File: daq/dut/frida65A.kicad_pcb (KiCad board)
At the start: 4 copper layers, 100 x 100 mm, 64 parts, among them J1 TP_PWR, J10 TP_LOGIC, J11 TP_OUT, J2 CONN_IN_P, J3 CONN_IN_N, J4 TP_CFG, J5 CONN_CFG, J6 TP_IN, J7 TP_INIT, J8 TP_SAMP, J9 TP_COMP, U1 DUT, U2 THS4520RGTT

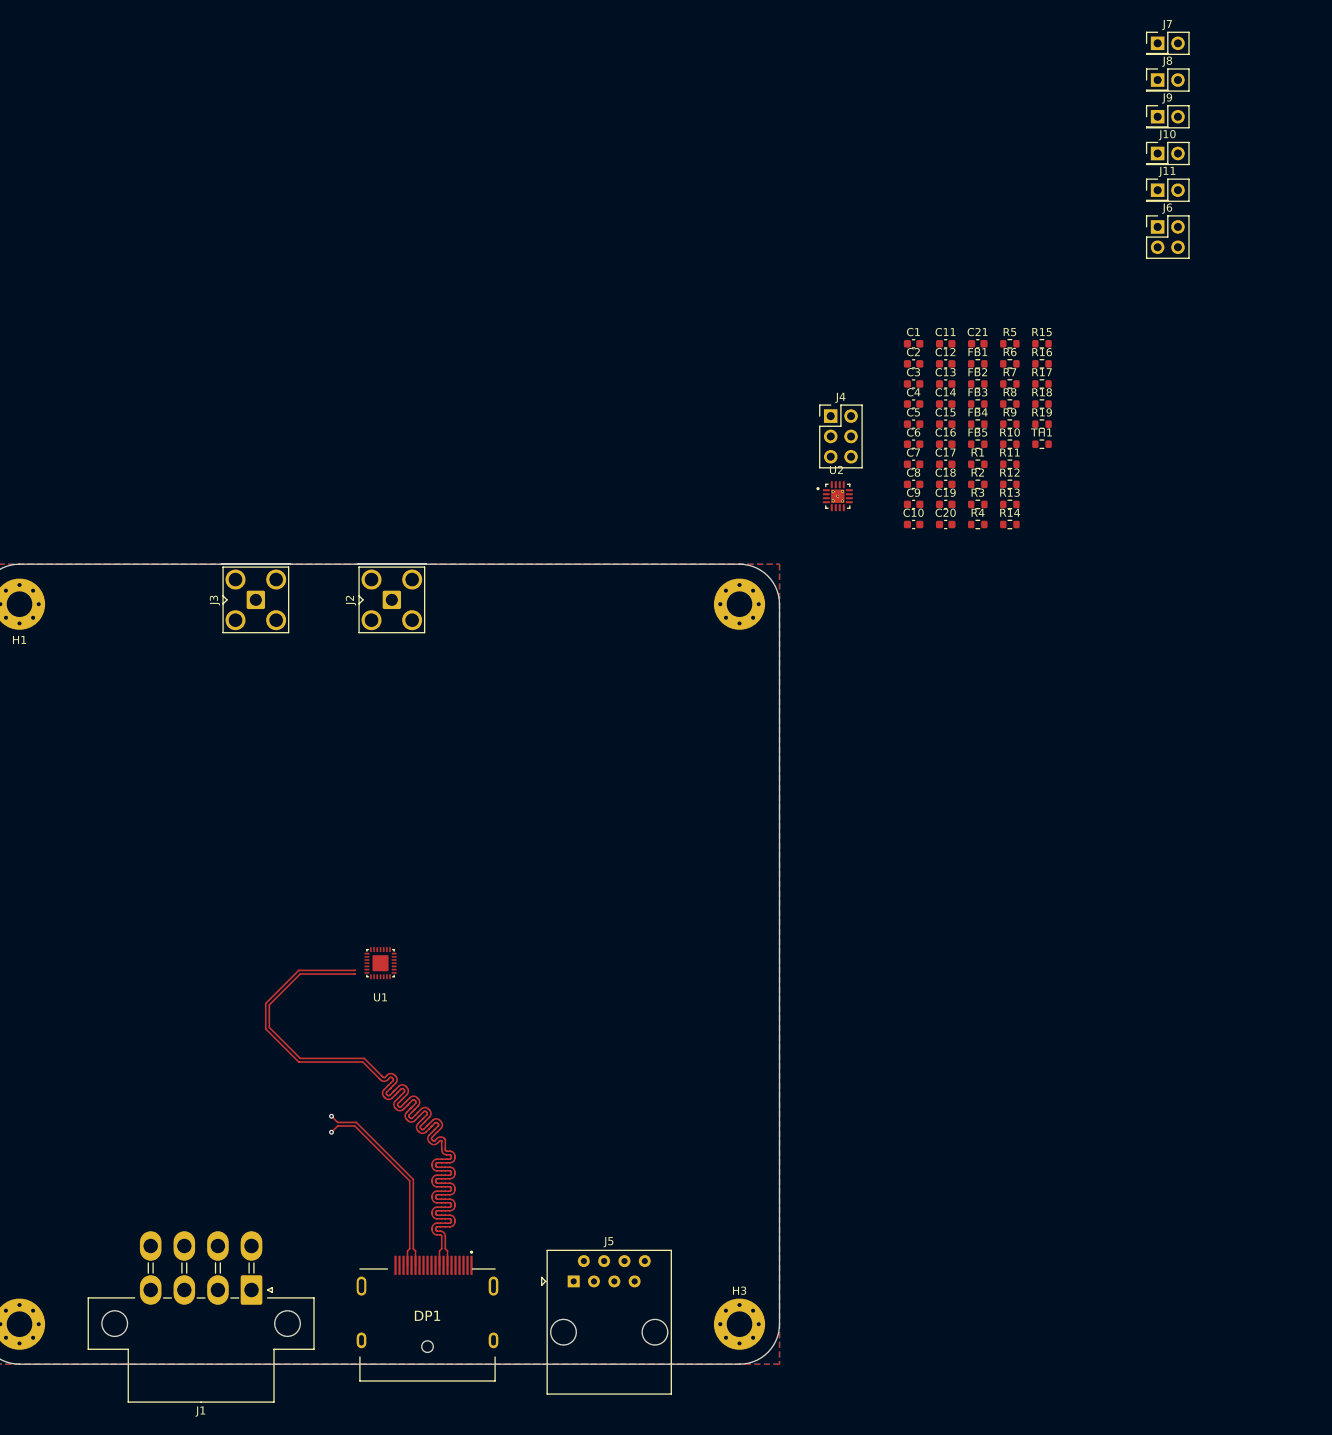
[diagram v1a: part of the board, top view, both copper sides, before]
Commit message: Update PCB schematic, and differential layout traces
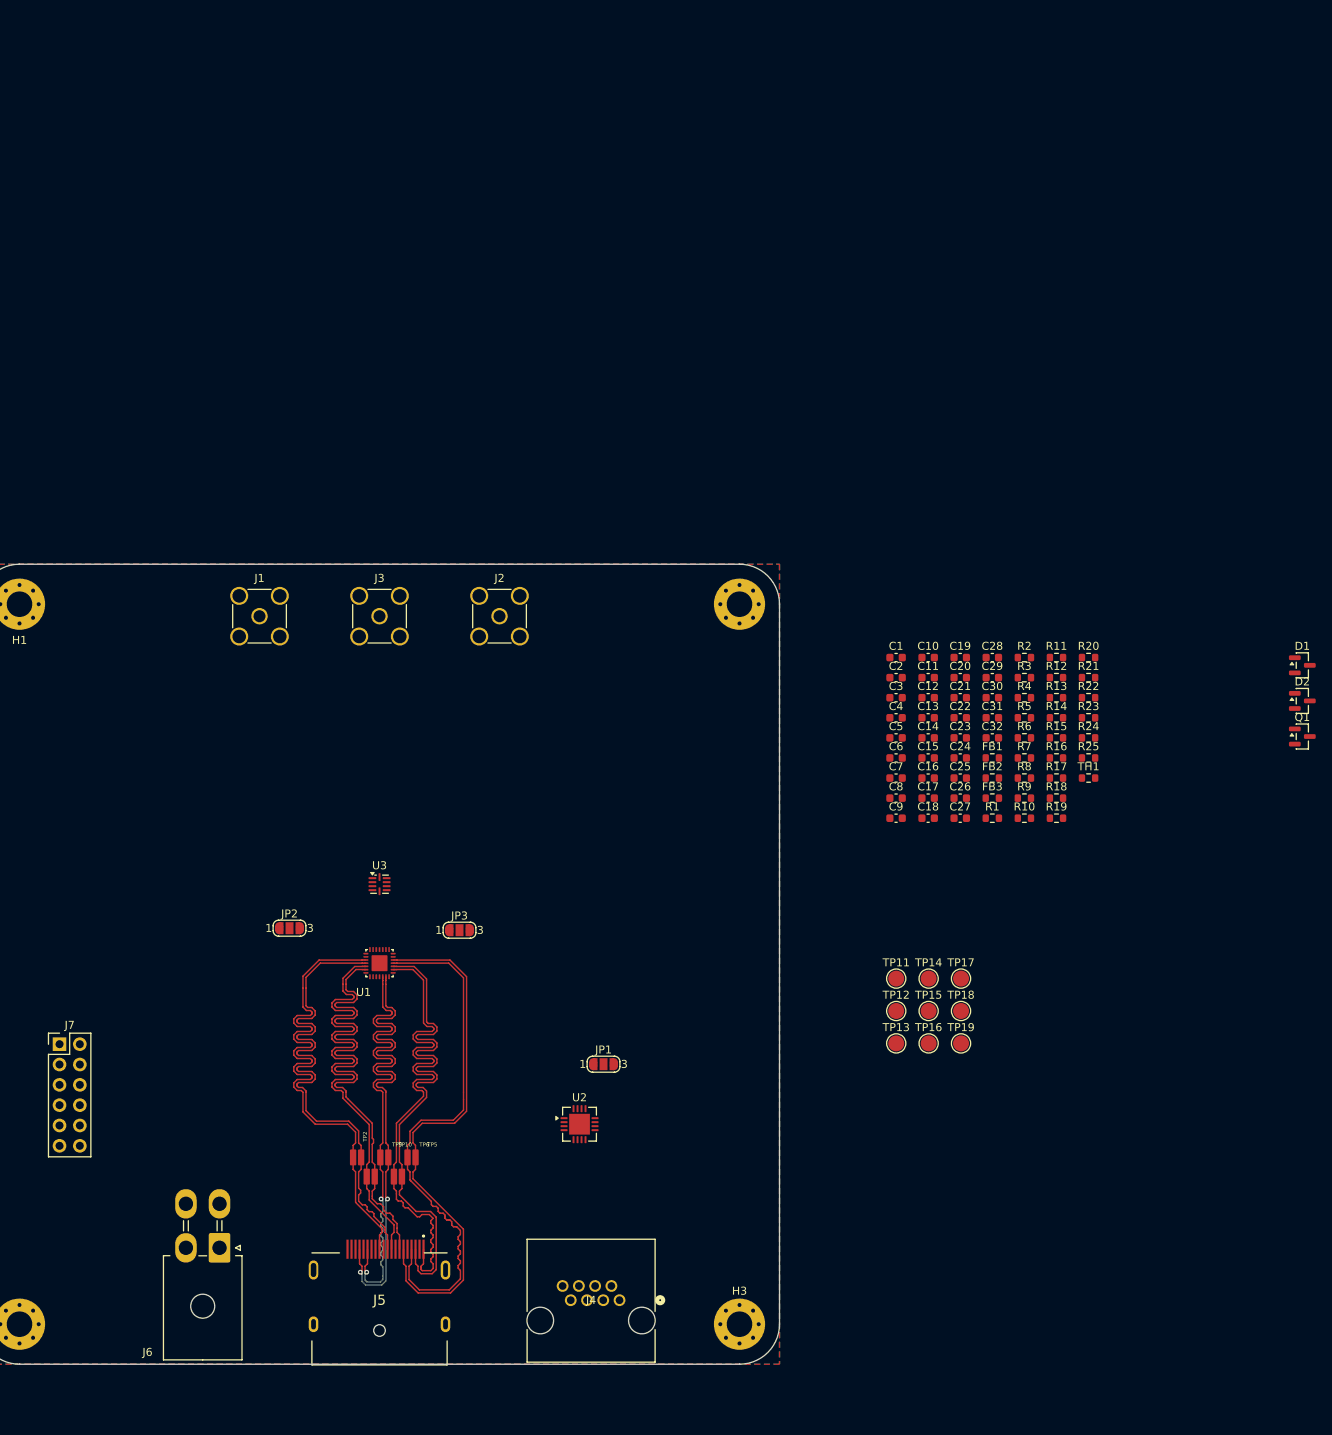
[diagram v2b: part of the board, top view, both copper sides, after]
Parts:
- removed DP1: DP, frida:Molex_DisplayPort_472720024
- removed FB4, FB5: FerriteBead_Small, Resistor_SMD:R_0603_1608Metric
- removed J10: TP_LOGIC, Connector_PinHeader_2.54mm:PinHeader_2x01_P2.54mm_Vertical
- removed J11: TP_OUT, Connector_PinHeader_2.54mm:PinHeader_2x01_P2.54mm_Vertical
- removed J8: TP_SAMP, Connector_PinHeader_2.54mm:PinHeader_2x01_P2.54mm_Vertical
- removed J9: TP_COMP, Connector_PinHeader_2.54mm:PinHeader_2x01_P2.54mm_Vertical
- added C22: 47u, Capacitor_SMD:C_0603_1608Metric, F.Cu at (222.6, 69.2)
- added C23: 1u, Capacitor_SMD:C_0603_1608Metric, F.Cu at (222.6, 71.7)
- added C24: 100n, Capacitor_SMD:C_0603_1608Metric, F.Cu at (222.6, 74.2)
- added C25: 100n, Capacitor_SMD:C_0603_1608Metric, F.Cu at (222.6, 76.7)
- added C26: 1u, Capacitor_SMD:C_0603_1608Metric, F.Cu at (222.6, 79.2)
- added C27: 100n, Capacitor_SMD:C_0603_1608Metric, F.Cu at (222.6, 81.8)
- added C28: 1u, Capacitor_SMD:C_0603_1608Metric, F.Cu at (226.6, 61.7)
- added C29: 100n, Capacitor_SMD:C_0603_1608Metric, F.Cu at (226.6, 64.2)
- added C30: 51pF, Capacitor_SMD:C_0603_1608Metric, F.Cu at (226.6, 66.7)
- added C31: 100n, Capacitor_SMD:C_0603_1608Metric, F.Cu at (226.6, 69.2)
- added C32: 1u, Capacitor_SMD:C_0603_1608Metric, F.Cu at (226.6, 71.7)
- added D1: BAV99, Package_TO_SOT_SMD:SOT-23, F.Cu at (265.4, 62.6)
- added D2: BAV99, Package_TO_SOT_SMD:SOT-23, F.Cu at (265.4, 67.1)
- added JP1: SolderJumper_3_Open, Jumper:SolderJumper-3_P1.3mm_Open_RoundedPad1.0x1.5mm_NumberLabels, F.Cu at (178.0, 112.5)
- added JP2: SolderJumper_3_Open, Jumper:SolderJumper-3_P1.3mm_Open_RoundedPad1.0x1.5mm_NumberLabels, F.Cu at (138.8, 95.5)
- added JP3: SolderJumper_3_Open, Jumper:SolderJumper-3_P1.3mm_Open_RoundedPad1.0x1.5mm_NumberLabels, F.Cu at (160.0, 95.8)
- added Q1: NMOS, Package_TO_SOT_SMD:SOT-23, F.Cu at (265.4, 71.5)
- added R20: 1k, Resistor_SMD:R_0603_1608Metric, F.Cu at (238.6, 61.7)
- added R21: 1k, Resistor_SMD:R_0603_1608Metric, F.Cu at (238.6, 64.2)
- added R22: 499, Resistor_SMD:R_0603_1608Metric, F.Cu at (238.6, 66.7)
- added R23: 499, Resistor_SMD:R_0603_1608Metric, F.Cu at (238.6, 69.2)
- added R24: 499, Resistor_SMD:R_0603_1608Metric, F.Cu at (238.6, 71.7)
- added R25: 499, Resistor_SMD:R_0603_1608Metric, F.Cu at (238.6, 74.2)
- added TP1: TestPoint Keystone 5001, frida:Test_Point, F.Cu at (146.7, 124.2)
- added TP10: TestPoint Keystone 5001, frida:Test_Point, F.Cu at (151.1, 124.2)
- added TP11: TestPoint, TestPoint:TestPoint_Pad_D2.0mm, F.Cu at (214.6, 101.8)
- added TP12: TestPoint, TestPoint:TestPoint_Pad_D2.0mm, F.Cu at (214.6, 105.8)
- added TP13: TestPoint, TestPoint:TestPoint_Pad_D2.0mm, F.Cu at (214.6, 109.9)
- added TP14: TestPoint, TestPoint:TestPoint_Pad_D2.0mm, F.Cu at (218.6, 101.8)
- added TP15: TestPoint, TestPoint:TestPoint_Pad_D2.0mm, F.Cu at (218.6, 105.8)
- added TP16: TestPoint, TestPoint:TestPoint_Pad_D2.0mm, F.Cu at (218.6, 109.9)
- added TP17: TestPoint, TestPoint:TestPoint_Pad_D2.0mm, F.Cu at (222.7, 101.8)
- added TP18: TestPoint, TestPoint:TestPoint_Pad_D2.0mm, F.Cu at (222.7, 105.8)
- added TP19: TestPoint, TestPoint:TestPoint_Pad_D2.0mm, F.Cu at (222.7, 109.9)
- added TP2: TestPoint Keystone 5001, frida:Test_Point, F.Cu at (147.7, 124.2)
- added TP3: TestPoint Keystone 5001, frida:Test_Point, F.Cu at (148.4, 126.5)
- added TP4: TestPoint Keystone 5001, frida:Test_Point, F.Cu at (149.4, 126.5)
- added TP5: TestPoint Keystone 5001, frida:Test_Point, F.Cu at (154.5, 124.2)
- added TP6: TestPoint Keystone 5001, frida:Test_Point, F.Cu at (153.5, 124.2)
- added TP7: TestPoint Keystone 5001, frida:Test_Point, F.Cu at (152.8, 126.5)
- added TP8: TestPoint Keystone 5001, frida:Test_Point, F.Cu at (151.8, 126.5)
- added TP9: TestPoint Keystone 5001, frida:Test_Point, F.Cu at (150.1, 124.2)
- added U3: DiffAmp TI THS4541, frida:TI_DiffAmp_THS4541, F.Cu at (150.0, 90.0)
- J1: value TP_PWR -> SMA Molex 733910070; footprint frida:Molex_MiniFitJr_469990014 -> frida:Molex_SMA_733910070
- J2: value CONN_IN_P -> SMA Molex 733910070; footprint Connector_Coaxial:SMA_Amphenol_901-143_Horizontal -> frida:Molex_SMA_733910070
- J3: value CONN_IN_N -> SMA Molex 733910070; footprint Connector_Coaxial:SMA_Amphenol_901-143_Horizontal -> frida:Molex_SMA_733910070
- J4: value TP_CFG -> RJ45 Molex 446200002; footprint Connector_PinHeader_2.54mm:PinHeader_2x03_P2.54mm_Vertical -> frida:Molex_RJ45_446200002
- J5: value CONN_CFG -> DisplayPort Molex 472720024; footprint Connector_RJ:RJ45_Amphenol_54602-x08_Horizontal -> frida:Molex_DisplayPort_472720024
- J6: value TP_IN -> MiniFitJr Molex 469990014; footprint Connector_PinHeader_2.54mm:PinHeader_2x02_P2.54mm_Vertical -> frida:Molex_MiniFitJr_469990014
- J7: value TP_INIT -> Conn_02x06_Top_Bottom; footprint Connector_PinHeader_2.54mm:PinHeader_2x01_P2.54mm_Vertical -> Connector_PinHeader_2.54mm:PinHeader_2x06_P2.54mm_Vertical
- R14, R15: value 499 -> 54.9
- R16: value 499 -> 10k
- R17: value 499 -> 50
- R18, R19: value 1k -> 499
- U1: value DUT -> ASIC FRIDA 65A
- U2: value THS4520RGTT -> LevelShifter TI TXV0106Q1; footprint frida:QFN50P300X300X100-17N -> frida:TI_LevelShifter_TXV0106Q1
- moved J7 185.7 mm to (110.0, 110.0)
- moved J6 173.3 mm to (130.0, 135.4), turned to 180 degrees
- moved J4 113.6 mm to (180.0, 142.0)
- moved U2 84.9 mm to (175.0, 120.0)
- moved J1 84.2 mm to (135.0, 56.5), turned to 0 degrees
- moved FB2 49.3 mm to (226.6, 76.7)
- moved R17 49.3 mm to (234.6, 76.7)
- moved FB1 49.3 mm to (226.6, 74.2)
- moved R16 49.3 mm to (234.6, 74.2)
- moved R19 49.3 mm to (234.6, 81.8)
- moved FB3 49.3 mm to (226.6, 79.2)
- moved R15 49.3 mm to (234.6, 71.7)
- moved R18 49.3 mm to (234.6, 79.2)
- moved R10 46.8 mm to (230.6, 81.8)
- moved R5 46.8 mm to (230.6, 69.2)
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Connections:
- C18 pad 1: /VDD_DIF -> /VS_N
- C19 pad 1: /VDD_DIF -> /VS_N
- C20 pad 1: /VDD_DIF -> /VS_N
- C21 pad 1: /VDD_DIF -> /VS_N
- FB1 pad 1: Net-(J17-Pin_1) -> Net-(FB1-Pad1)
- FB1 pad 2: /VDD_D -> /VDD
- FB2 pad 1: Net-(J17-Pin_2) -> Net-(FB2-Pad1)
- FB2 pad 2: /VDD_A -> Net-(J7-Pin_5)
- FB3 pad 1: Net-(J17-Pin_3) -> Net-(FB3-Pad1)
- FB3 pad 2: /VDD_DAC -> Net-(J7-Pin_6)
- J1 pad 1: /VDD_D -> GND
- J1 pad 2: /VDD_A -> /VIN_P_EXT
- J2 pad 1: /VIN_P_EXT -> GND
- J2 pad 2: GND -> /VIN_N_EXT
- J3 pad 1: /VIN_N_EXT -> GND
- J3 pad 2: GND -> /VOCM_EXT
- J4 pad 1: /SPI_CS_B -> /SPI_CS_B_EXT
- J4 pad 2: /SPI_SDO -> /SPI_SDO_EXT
- J4 pad 3: /SPI_SDI -> /SPI_SDI_EXT
- J4 pad 4: /SPI_SCLK -> /SPI_SCLK_EXT
- J4 pad 5: /RST_B -> /RST_B_EXT
- J4 pad 6: GND -> /AMP_EN_EXT_B
- J5 pad 1: /SPI_CS_B -> /CLK_LOGIC_N
- J5 pad 2: /SPI_SDO -> GND
- J5 pad 3: /SPI_SDI -> /CLK_LOGIC_P
- J5 pad 4: /SPI_SCLK -> /CLK_COMP_N
- J5 pad 5: /RST_B -> GND
- J5 pad 6: /AMP_EN -> /CLK_COMP_P
- J5 pad 7: unconnected-(J5-Pad7) -> /CLK_SAMP_N
- J5 pad 8: unconnected-(J5-Pad8) -> GND
- J6 pad 1: Net-(J16-Pin_3) -> Net-(FB1-Pad1)
- J6 pad 2: Net-(J16-Pin_3) -> Net-(FB2-Pad1)
- J6 pad 3: GND -> Net-(FB3-Pad1)
- J7 pad 1: /CLK_INIT_P -> /VDD
- J7 pad 2: /CLK_INIT_N -> /VDD
- R10 pad 1: /CLK_COMP_N -> /CLK_SAMP_P
- R11 pad 1: /CLK_LOGIC_P -> /CLK_INIT_N
- R12 pad 1: /CLK_LOGIC_N -> /CLK_INIT_P
- R14 pad 1: Net-(U2-VIN-) -> GND
- R14 pad 2: Net-(J12-Pin_1) -> /VIN_P_EXT
- R15 pad 1: Net-(U2-VIN+) -> GND
- R15 pad 2: Net-(J16-Pin_1) -> Net-(JP1-C)
- R16 pad 1: unconnected-(R16-Pad1) -> /VS_P
- R16 pad 2: Net-(U2-VIN+) -> /AMP_EN
- R17 pad 1: unconnected-(R17-Pad1) -> GND
- R17 pad 2: Net-(U2-VIN-) -> Net-(JP1-A)
- R18 pad 1: GND -> Net-(U3-IN-)
- R18 pad 2: /AMP_EN -> Net-(JP1-C)
- R19 pad 1: Net-(U2-~{PD}) -> Net-(U3-IN+)
- R19 pad 2: GND -> /VIN_P_EXT
- R5 pad 1: /CLK_INIT_P -> /CLK_LOGIC_N
- R6 pad 1: /CLK_INIT_N -> /CLK_LOGIC_P
- R7 pad 1: /CLK_SAMP_P -> /CLK_COMP_N
- R8 pad 1: /CLK_SAMP_N -> /CLK_COMP_P
- R9 pad 1: /CLK_COMP_P -> /CLK_SAMP_N
- TH1 pad 1: Net-(DP1-Pad13) -> Net-(J5-Pad13)
- TH1 pad 2: Net-(DP1-Pad14) -> Net-(J5-Pad14)
- U1 pad 24: Net-(J16-Pin_3) -> /VIN_N
- U1 pad 25: Net-(J12-Pin_3) -> /VIN_P
- U2 pad 1: (no net) -> /VDD_DAQ
- U2 pad 10: Net-(J16-Pin_1) -> unconnected-(U2-B6-Pad10)
- U2 pad 11: Net-(U2-VIN+) -> /SPI_CS_B
- U2 pad 12: Net-(U2-~{PD}) -> /SPI_SDO
- U2 pad 13: GND -> /SPI_SDI
- U2 pad 14: GND -> /SPI_SCLK
- U2 pad 15: GND -> /RST_B
- U2 pad 16: GND -> /VDD_IO
- U2 pad 2: Net-(U2-VIN-) -> /RST_B_EXT
- U2 pad 3: Net-(J12-Pin_1) -> /SPI_SCLK_EXT
- U2 pad 4: unconnected-(U2-CM-Pad4) -> /SPI_SDI_EXT
- U2 pad 5: /VDD_DIF -> /SPI_SDO_EXT
- U2 pad 6: /VDD_DIF -> /SPI_CS_B_EXT
- U2 pad 7: /VDD_DIF -> unconnected-(U2-A6-Pad7)
- U2 pad 8: /VDD_DIF -> GND
- U2 pad 9: unconnected-(U2-CM__1-Pad9) -> GND
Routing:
- net /CLK_COMP_P: track 0.00 -> 68.5 mm
- net /CLK_INIT_N: track 0.00 -> 68.5 mm
- net /CLK_COMP_N: track 0.00 -> 68.5 mm
- net /CLK_INIT_P: track 0.00 -> 68.5 mm
- net /CLK_LOGIC_N: track 0.00 -> 68.5 mm
- net /CLK_LOGIC_P: track 0.00 -> 68.5 mm
- net /CLK_SAMP_P: track 99.3 -> 68.5 mm
- net /CLK_SAMP_N: track 98.5 -> 68.5 mm
- net /COMP_OUT_N: track 44.9 -> 65.4 mm, vias 1 -> 2
- net /COMP_OUT_P: track 45.3 -> 65.4 mm, vias 1 -> 2

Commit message: Remove solder mask from footprints
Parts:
- J7: value Conn_02x06_Top_Bottom -> Conn_02x06_Odd_Even
- moved J7 25.6 mm to (85.5, 117.3)
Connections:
- FB2 pad 2: Net-(J7-Pin_5) -> Net-(J7-Pin_9)
- FB3 pad 2: Net-(J7-Pin_6) -> Net-(J7-Pin_11)
- J7 pad 10: /VDD_DAC -> /VS_P
- J7 pad 11: /VS_P -> Net-(J7-Pin_11)
- J7 pad 2: /VDD -> /VDD_A
- J7 pad 4: /VDD -> /VDD_IO
- J7 pad 5: Net-(J7-Pin_5) -> /VDD
- J7 pad 6: Net-(J7-Pin_6) -> /VDD_D
- J7 pad 7: /VDD_A -> /VDD
- J7 pad 8: /VDD_IO -> /VDD_DAC
- J7 pad 9: /VDD_D -> Net-(J7-Pin_9)

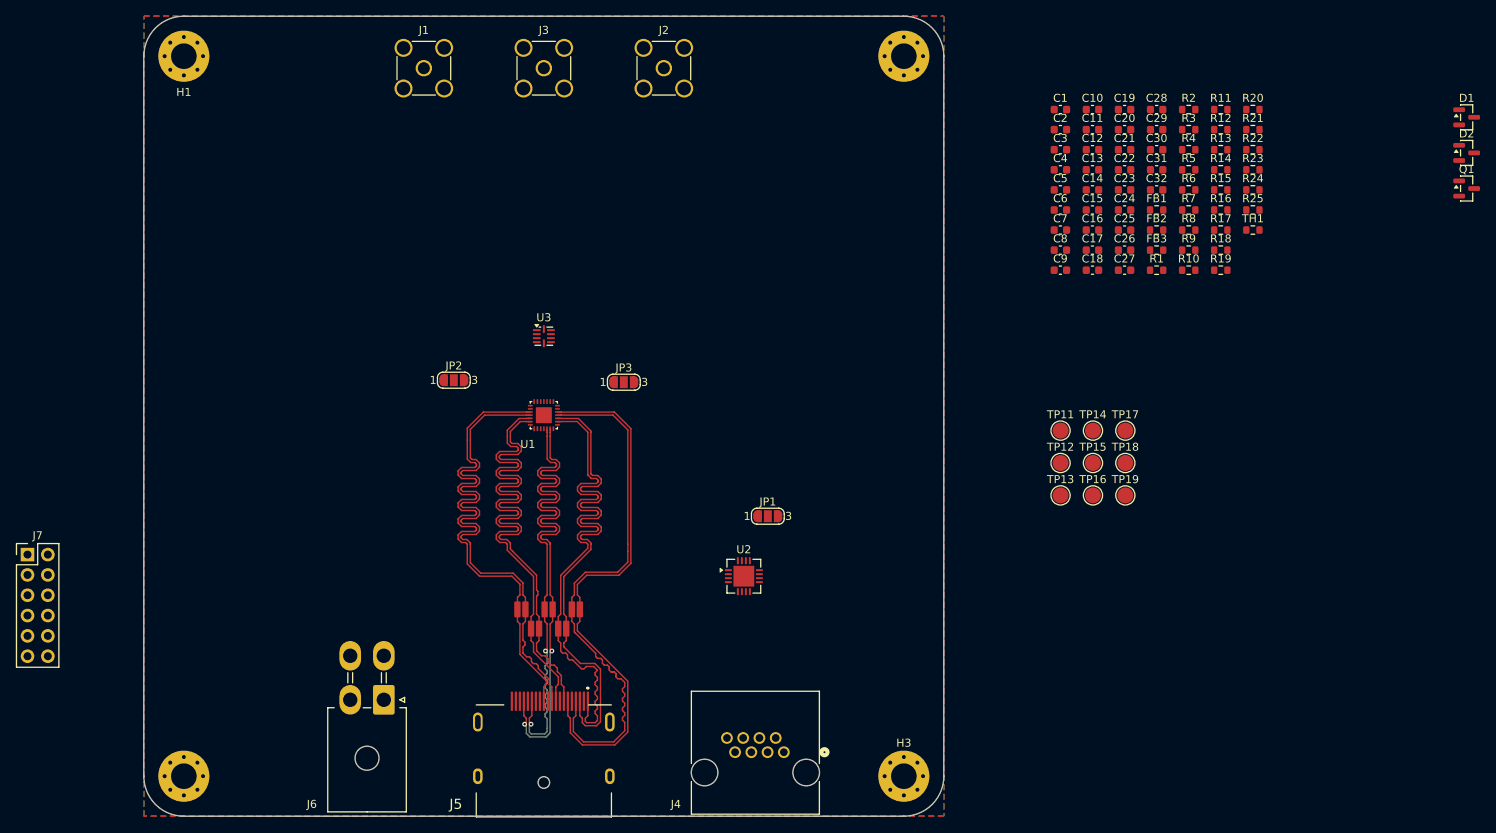
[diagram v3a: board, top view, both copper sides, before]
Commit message: Updated pcb layout, added some todo
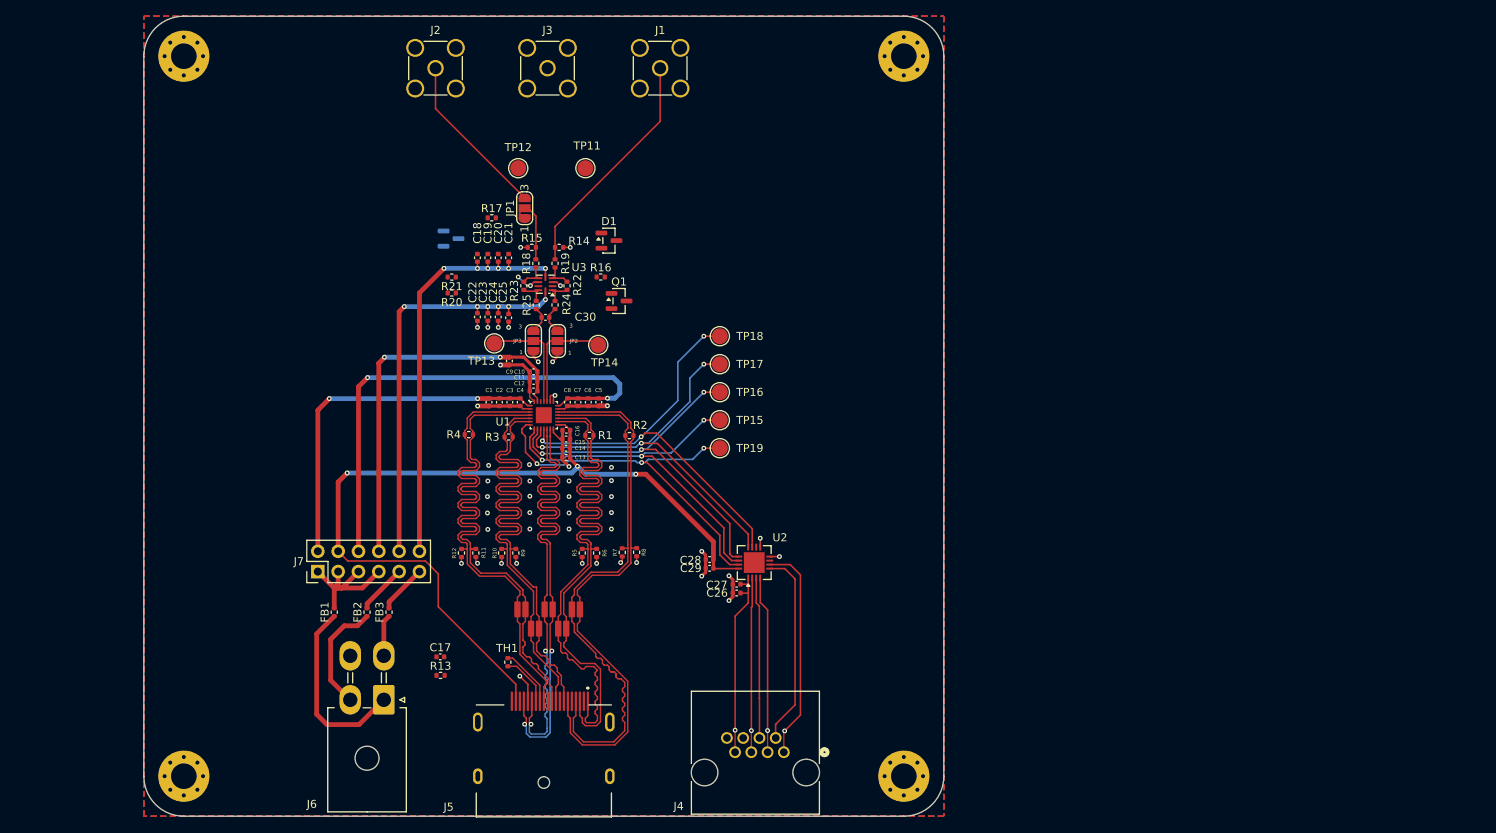
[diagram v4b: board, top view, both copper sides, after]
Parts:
- removed C31: 100n, Capacitor_SMD:C_0603_1608Metric
- removed C32: 1u, Capacitor_SMD:C_0603_1608Metric
- C1, C10, C11, C12, C13, C14, C15, C16, C17, C18, C19, C2, C20, C21, C22, C23, C24, C25, C26, C27, C28, C29, C3, C30, C4, C5, C6, C7, C8, C9: footprint Capacitor_SMD:C_0603_1608Metric -> Capacitor_SMD:C_0402_1005Metric
- D2: moved to B.Cu
- FB1, FB2, FB3, R1, R10, R11, R12, R13, R14, R15, R16, R17, R18, R19, R2, R20, R21, R22, R23, R24, R25, R3, R4, R5, R6, R7, R8, R9, TH1: footprint Resistor_SMD:R_0603_1608Metric -> Resistor_SMD:R_0402_1005Metric
- moved D2 127.4 mm to (138.4, 77.8)
- moved R13 117.6 mm to (137.1, 132.4)
- moved FB1 114.4 mm to (123.8, 124.5), turned to 90 degrees
- moved FB2 109.7 mm to (127.9, 124.5), turned to 90 degrees
- moved R12 108.7 mm to (139.7, 117.1), turned to -90 degrees
- moved R11 108.4 mm to (141.5, 117.1), turned to -90 degrees
- moved D1 108.3 mm to (158.1, 78.0)
- moved TH1 107.7 mm to (145.5, 130.8), turned to -90 degrees
- moved Q1 106.9 mm to (159.4, 85.6)
- moved FB3 106.1 mm to (130.7, 124.5), turned to 90 degrees
- moved R20 102.7 mm to (138.5, 84.6), turned to 180 degrees
- moved R21 101.8 mm to (138.5, 82.6), turned to 180 degrees
- moved R4 96.8 mm to (140.6, 102.3), turned to 180 degrees
- moved C17 96.1 mm to (137.1, 130.1)
- moved R3 93.3 mm to (145.6, 102.6), turned to 180 degrees
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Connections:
- J1 pad 1: GND -> /VIN_P_EXT
- J1 pad 2: /VIN_P_EXT -> GND
- J2 pad 1: GND -> /VIN_N_EXT
- J2 pad 2: /VIN_N_EXT -> GND
- J3 pad 1: GND -> /VOCM_EXT
- J3 pad 2: /VOCM_EXT -> GND
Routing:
- net /VDD_IO: track 0.00 -> 107.2 mm, vias 0 -> 3
- net /VDD_D: track 0.00 -> 63.7 mm, vias 0 -> 2
- net GND: track 0.00 -> 54.4 mm, vias 0 -> 45
- net /VS_N: track 0.00 -> 53.9 mm, vias 0 -> 6
- net /VS_P: track 0.00 -> 53.6 mm, vias 0 -> 6
- net /SPI_CS_B: track 0.00 -> 53.6 mm, vias 0 -> 3
- net /SPI_SDO: track 0.00 -> 51.0 mm, vias 0 -> 3
- net /RST_B: track 0.00 -> 49.4 mm, vias 0 -> 3
- net /SPI_SDI: track 0.00 -> 49.3 mm, vias 0 -> 3
- net /VDD_DAC: track 0.00 -> 48.6 mm, vias 0 -> 2
- net /SPI_SCLK: track 0.00 -> 48.4 mm, vias 0 -> 3
- net /VDD_A: track 0.00 -> 45.2 mm, vias 0 -> 2
- net /VIN_P_EXT: track 0.00 -> 31.4 mm, vias 0 -> 1
- net /SPI_CS_B_EXT: track 0.00 -> 27.4 mm, vias 0 -> 1
- net /SPI_SDO_EXT: track 0.00 -> 24.6 mm
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- added copper zone on In1.Cu, net GND
- added copper zone on In2.Cu, net GND
